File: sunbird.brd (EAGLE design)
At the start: 111 x 19.1 mm, 68 parts, among them J1 USB_MINI-B_SMT, Q8010 600mA/40V, U1000 TP4056, U1500 FS312F-G, U1550 FS8205, U2000 MT3608, U2100 M3406, U4000 FM116B, U5000 CH340G, U6000 RICHTEK-RT3000CGQM, U6001 0.1uF, U6100 HDC1080NOPAD, Y5000 12Mhz

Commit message: Adding image exports
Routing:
- net V_USB_UNFUSED: track 79.7 -> 79.2 mm

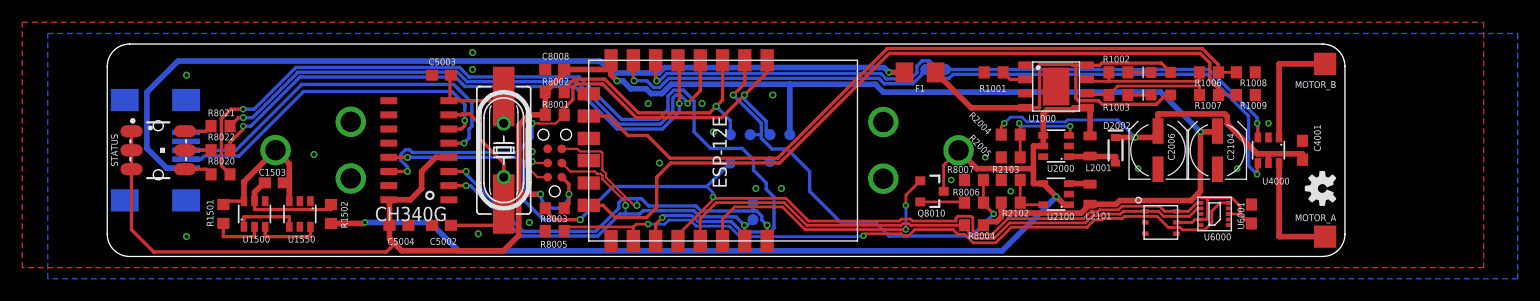
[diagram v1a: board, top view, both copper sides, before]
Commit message: Revise PCB to use inductors + 47uF 0603 "miracle" caps from LCSC.
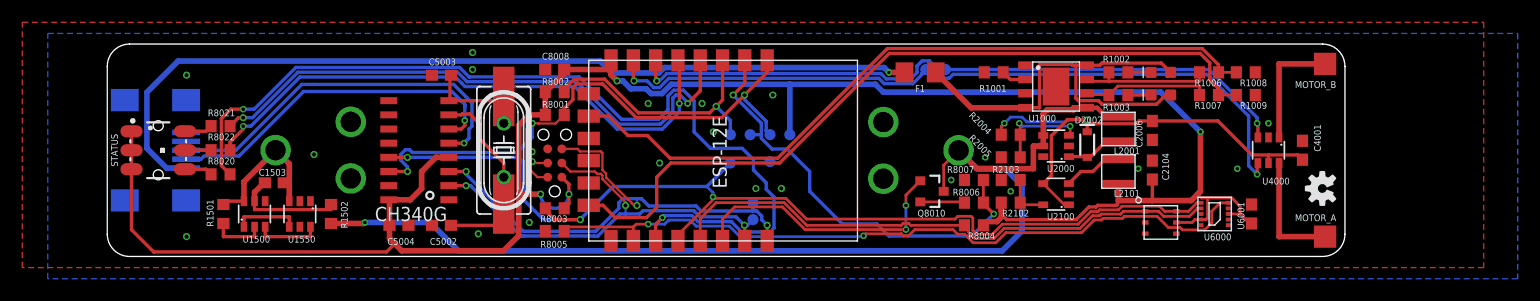
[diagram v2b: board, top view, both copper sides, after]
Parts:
- C2006, C2104: device rcl:UD-5X5,8_NICHICON -> rcl:C0603
- L2001, L2101: device SparkFun-Coils:0805 -> geusebio:INDUCTOR_3.0X3.0
- U1000: device geusebio:SOP-8 -> geusebio:SOP-8-THERMAL
- moved C2104 6.11 mm to (93.7, 7.75)
- moved L2101 3.25 mm to (90.7, 7.62)
- moved L2001 2.96 mm to (90.7, 11.4)
- moved D2002 2.59 mm to (87.9, 10.0)
- moved C2006 1.85 mm to (93.7, 11.3), turned to 270 degrees
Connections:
- net 3.3V: now also C2104.1, L2101.P$2; no longer C2104.+, L2101.2
- net 5V: now also C2006.1, U2100.1, U2100.4; no longer C2006.+
- net BUCK: now also L2001.P$2; no longer L2001.2
- net GND: now also C2006.2, C2104.2; no longer C2006.-, C2104.-
- net N$1: now also L2101.P$1; no longer L2101.1
- net V_BATT: now also L2001.P$1; no longer L2001.1, U2100.1, U2100.4
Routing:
- net 5V: track 36.1 -> 43.3 mm
- net 3.3V: track 190.2 -> 193.6 mm
- net N$1: track 1.95 -> 5.35 mm
- net V_BATT: track 97.9 -> 100.0 mm, vias 2 -> 1

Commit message: Removing sensor array
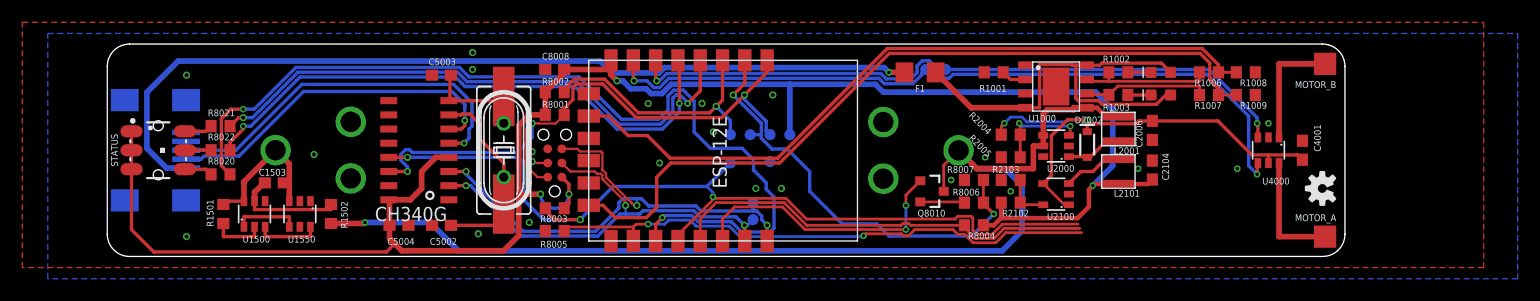
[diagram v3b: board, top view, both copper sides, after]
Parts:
- removed U6000: RICHTEK-RT3000CGQM, geusebio:MDFN-10L_3X3
- removed U6001: 0.1uF, rcl:C0603
- removed U6100: HDC1080NOPAD, geusebio:WSON6_NOPAD
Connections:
- net 3.3V: no longer U6000.P$3, U6000.P$9, U6001.1, U6100.P$5
- net ACC_INT/GPIO15: no longer U6000.P$5
- net GND: no longer U6000.P$4, U6001.2, U6100.P$2
- net SCL/GPIO0: no longer U6000.P$6, U6100.P$6
- net SDA/GPIO4: no longer U6000.P$7, U6100.P$1
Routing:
- net 3.3V: track 193.6 -> 167.2 mm
- net ACC_INT/GPIO15: track 66.0 -> 50.2 mm
- net SCL/GPIO0: track 96.8 -> 84.6 mm
- net SDA/GPIO4: track 50.6 -> 38.6 mm

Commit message: Rejig layout, add measurement indexes
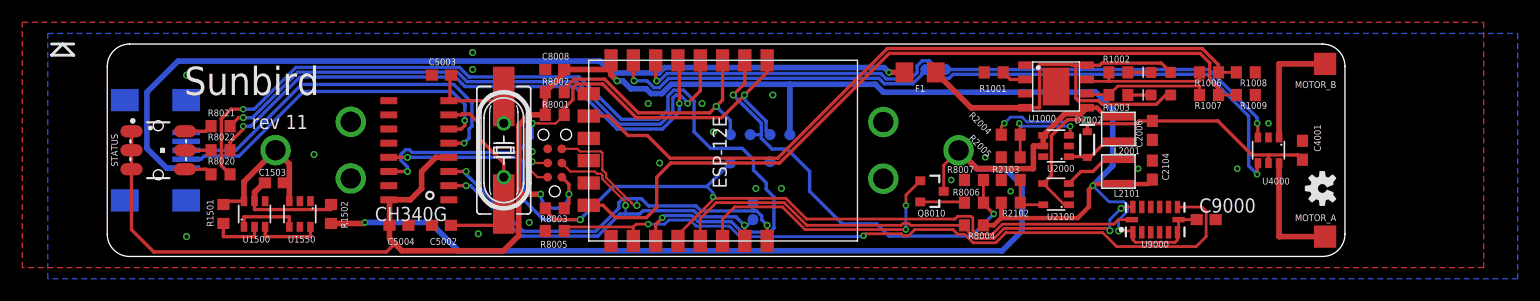
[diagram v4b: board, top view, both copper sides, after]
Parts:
- added C9000: 0.1uf, rcl:C0603
- added U9000: ADXL345, SparkFun-Sensors:LGA-14
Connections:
- net 3.3V: now also C9000.1, U9000.1, U9000.6, U9000.7
- net ACC_INT/GPIO15: now also U9000.8
- net GND: now also C9000.2, U9000.12, U9000.2, U9000.4, U9000.5
- net SCL/GPIO0: now also U9000.14
- net SDA/GPIO4: now also U9000.13
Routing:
- net ACC_INT/GPIO15: track 50.2 -> 67.2 mm
- net 3.3V: track 167.2 -> 183.4 mm, vias 4 -> 5
- net SDA/GPIO4: track 38.6 -> 44.9 mm, vias 0 -> 2
- net SCL/GPIO0: track 84.6 -> 89.6 mm
- net V_BATT: track 100.0 -> 98.4 mm
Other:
- board text added: "111mm"
- board text added: "19.05mm"
- board text added: "Sunbird"
- board text added: "rev 11"
